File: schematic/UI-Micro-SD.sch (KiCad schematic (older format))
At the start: 30 parts, among them IC1 TCA9534PWR, J1 47309-3351, J2 Conn_02x04_Odd_Even, J3 Conn_02x05_Odd_Even, J4 Conn_02x03_Odd_Even, J5 Conn_02x08_Odd_Even, J6 Conn_01x08, J7 Conn_02x08_Odd_Even, J8 Solder-Jumper-3-3-3-Open, Q1 BSS138, U1 SFV14R-2STE1HLF, U2 DizzyBITLogo, U3 DizzyBIT-Layout

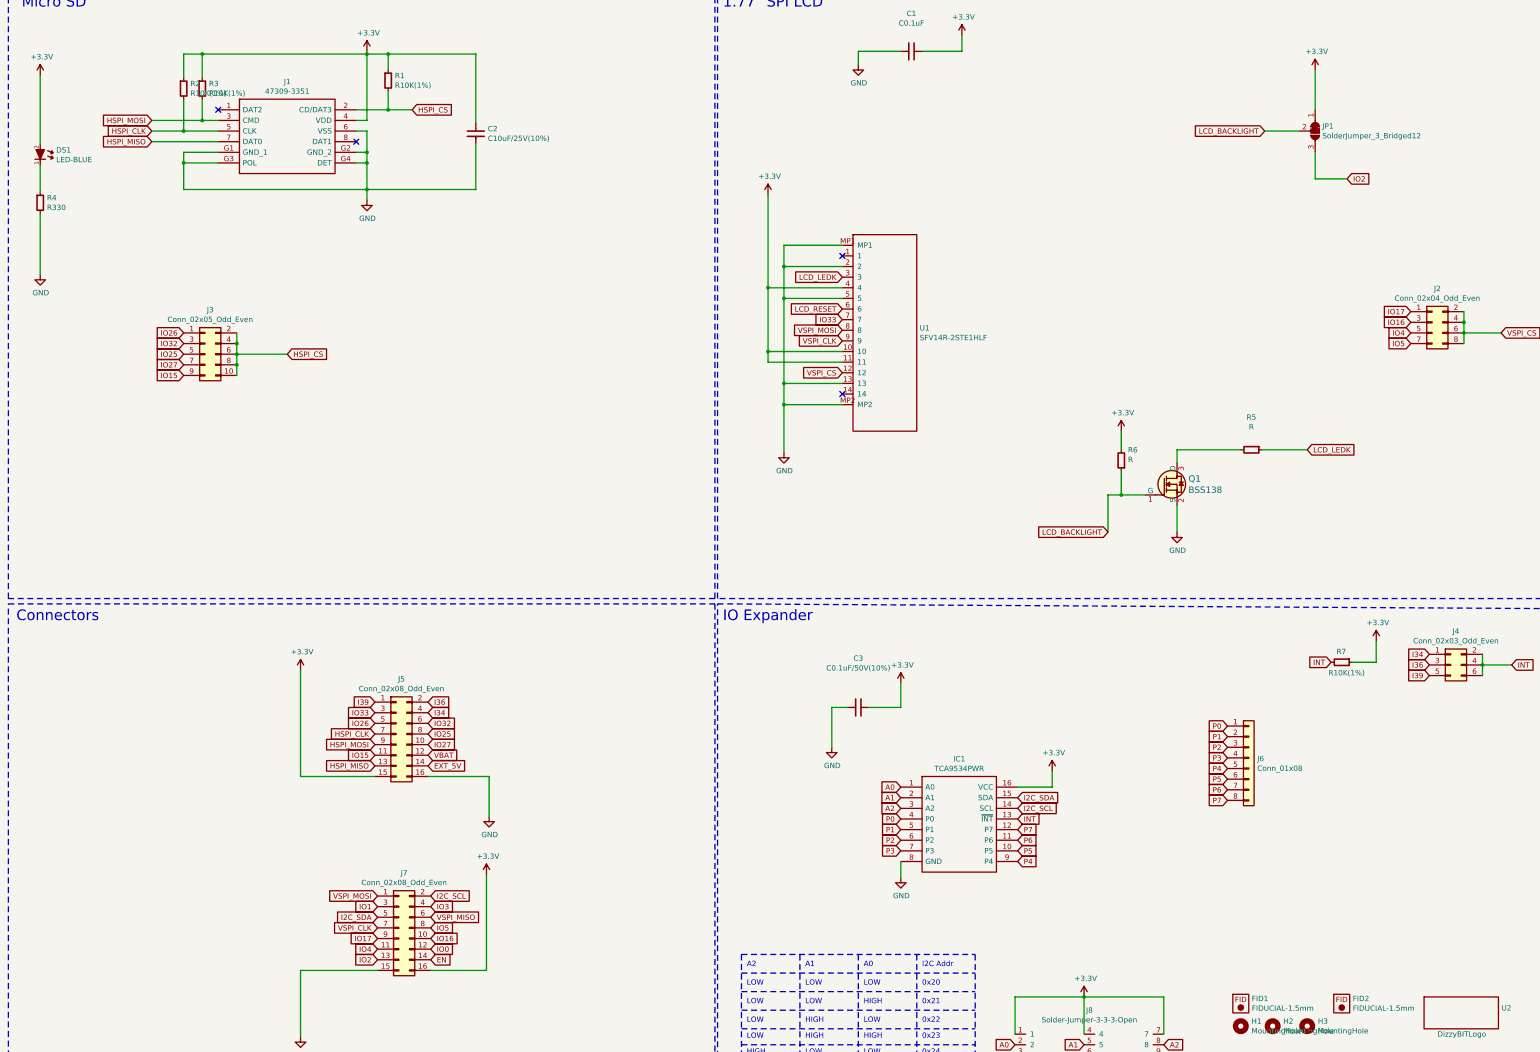
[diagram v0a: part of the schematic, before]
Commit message: Changed Connector designators
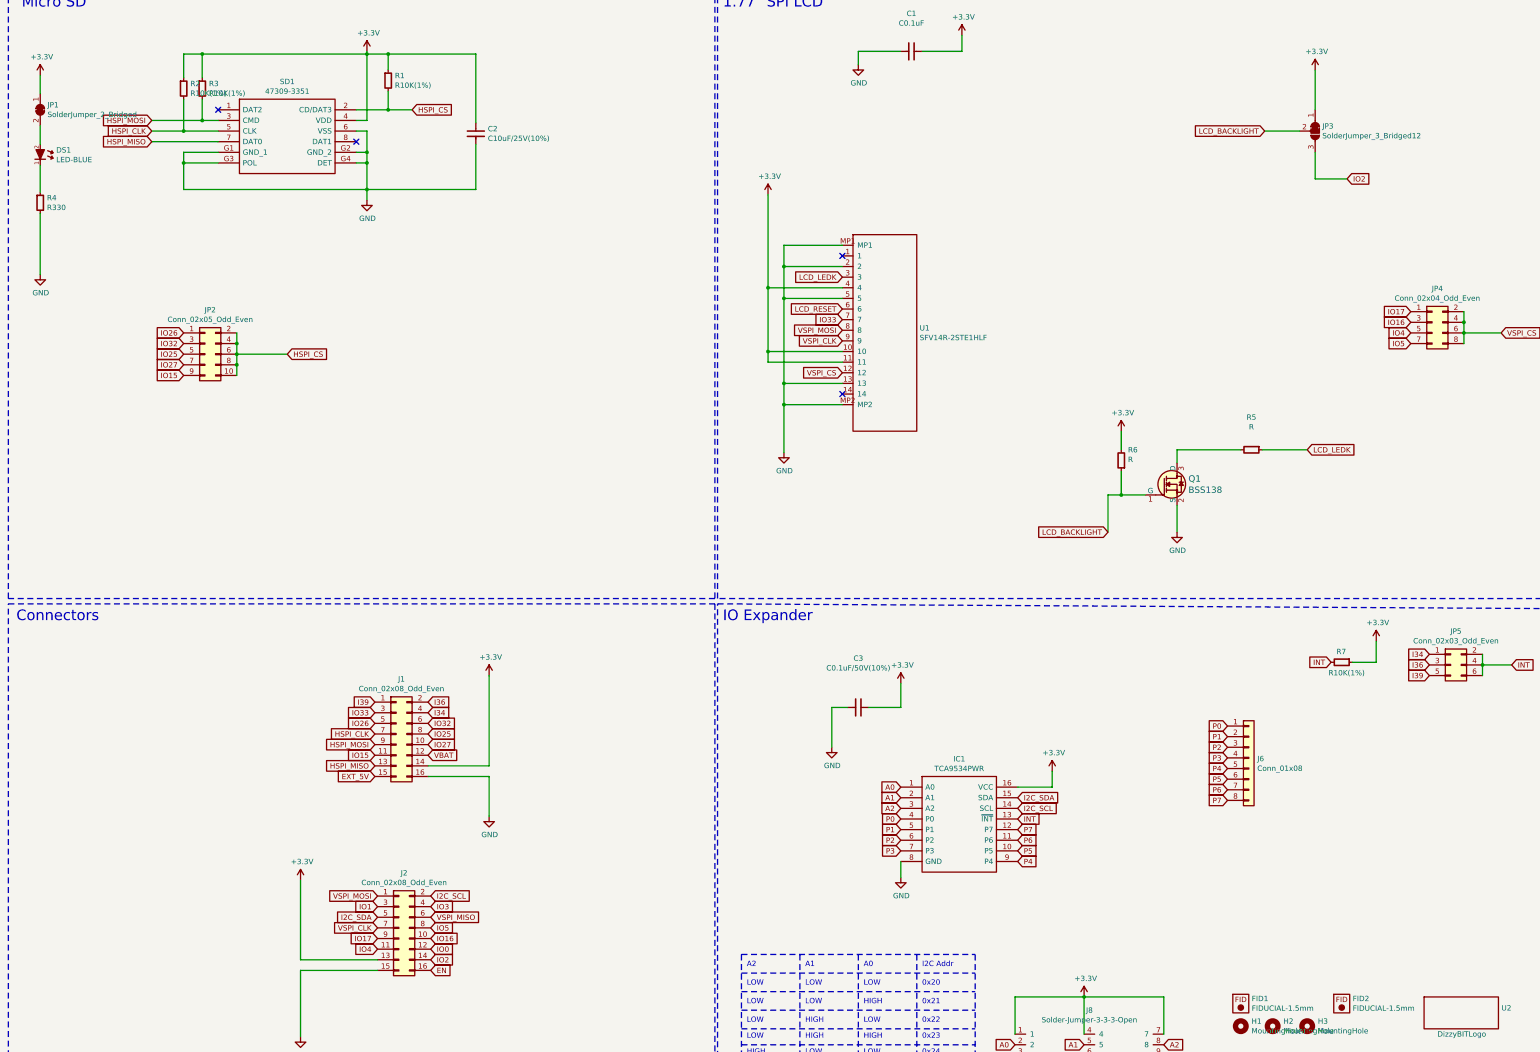
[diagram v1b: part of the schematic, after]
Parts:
- added JP1: SolderJumper_2_Bridged, symbol Jumper:SolderJumper_2_Bridged
- renumbered J5 to J1, J7 to J2, J3 to JP2, JP1 to JP3, J2 to JP4, J4 to JP5, J1 to SD1
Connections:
- net +3V3: now also J1.14 (Pin_14), J2.13 (Pin_13), JP1.1 (A); no longer DS1.2 (A), J1.15 (Pin_15), J2.16 (Pin_16)
- net EN: now also J2.16 (Pin_16); no longer J2.14 (Pin_14)
- net EXT_5V: now also J1.15 (Pin_15); no longer J1.14 (Pin_14)
- net IO2: now also J2.14 (Pin_14); no longer J2.13 (Pin_13)
- new net: DS1.2 (A), JP1.2 (B)
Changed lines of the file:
@@
 EESchema Schematic File Version 4
-LIBS:DizzyBit-MicroSD-cache
-LIBS:2-relay-over-io-cache
-LIBS:_DizzyBit-1.77LCD-cache
-LIBS:StandOut-2.0LCD-Keypad-cache
+LIBS:UI-Micro-SD-cache
 EELAYER 26 0
 EELAYER END
@@
 $EndComp
 Wire Wire Line
-	875  2050 875  1400
+	875  2050 875  1875
 $Comp
 L power:GND #PWR0102
@@
 	875  2250 875  2500
 $Comp
-L SamacSys_Parts:47309-3351 J1
+L SamacSys_Parts:47309-3351 SD1
 U 1 1 5C618E16
 P 2550 1725
-F 0 "J1" H 3200 1990 50  0000 C CNN
+F 0 "SD1" H 3200 1990 50  0000 C CNN
 F 1 "47309-3351" H 3200 1899 50  0000 C CNN
 F 2 "undo:Molex-MicroSD-473093351" H 3700 1825 50  0001 L CNN
@@
 VSPI_MOSI
 $Comp
-L Connector_Generic:Conn_02x08_Odd_Even J5
+L Connector_Generic:Conn_02x08_Odd_Even J1
 U 1 1 5D8B59AB
 P 4225 7600
-F 0 "J5" H 4275 8117 50  0000 C CNN
+F 0 "J1" H 4275 8117 50  0000 C CNN
 F 1 "Conn_02x08_Odd_Even" H 4275 8026 50  0000 C CNN
 F 2 "Connector_PinHeader_2.54mm:PinHeader_2x08_P2.54mm_Vertical" H 4225 7600 50  0001 C CNN
@@
 L power:+3.3V #PWR0105
 U 1 1 5D8B5B52
-P 3325 7000
-F 0 "#PWR0105" H 3325 6850 50  0001 C CNN
-F 1 "+3.3V" H 3340 7173 50  0000 C CNN
-F 2 "" H 3325 7000 50  0001 C CNN
-F 3 "" H 3325 7000 50  0001 C CNN
-	1    3325 7000
-	1    0    0    -1
-$EndComp
-Wire Wire Line
-	3325 8000 4025 8000
+P 5100 7050
+F 0 "#PWR0105" H 5100 6900 50  0001 C CNN
+F 1 "+3.3V" H 5115 7223 50  0000 C CNN
+F 2 "" H 5100 7050 50  0001 C CNN
+F 3 "" H 5100 7050 50  0001 C CNN
+	1    5100 7050
+	1    0    0    -1
+$EndComp
 $Comp
 L power:GND #PWR0106
@@
 L power:+3.3V #PWR0107
 U 1 1 5D8B5BF6
-P 5075 8925
-F 0 "#PWR0107" H 5075 8775 50  0001 C CNN
-F 1 "+3.3V" H 5090 9098 50  0000 C CNN
-F 2 "" H 5075 8925 50  0001 C CNN
-F 3 "" H 5075 8925 50  0001 C CNN
-	1    5075 8925
+P 3325 8975
+F 0 "#PWR0107" H 3325 8825 50  0001 C CNN
+F 1 "+3.3V" H 3340 9148 50  0000 C CNN
+F 2 "" H 3325 8975 50  0001 C CNN
+F 3 "" H 3325 8975 50  0001 C CNN
+	1    3325 8975
 	1    0    0    -1
 $EndComp
@@
 $EndComp
 Wire Wire Line
-	4550 9825 5075 9825
-Wire Wire Line
-	5075 9825 5075 8925
-Wire Wire Line
 	5100 8375 5100 8000
-Wire Wire Line
-	3325 8000 3325 7000
 Text GLabel 4050 9325 0    50   Input ~ 0
 I2C_SDA
@@
 Text GLabel 4050 9225 0    50   Input ~ 0
 IO1
-Text GLabel 4050 9725 0    50   Input ~ 0
+Text GLabel 4550 9725 2    50   Input ~ 0
 IO2
 Text GLabel 4550 9225 2    50   Input ~ 0
@@
 Text GLabel 4025 7300 0    50   Input ~ 0
 I39
-Text GLabel 4525 7900 2    50   Input ~ 0
+Text GLabel 4025 8000 0    50   Input ~ 0
 EXT_5V
 Wire Notes Line
@@
 Text GLabel 4525 7800 2    50   Input ~ 0
 VBAT
-Text GLabel 4550 9725 2    50   Input ~ 0
+Text GLabel 4550 9825 2    50   Input ~ 0
 EN
 $Comp
@@
 $EndComp
 $Comp
-L Connector_Generic:Conn_02x08_Odd_Even J7
+L Connector_Generic:Conn_02x08_Odd_Even J2
 U 1 1 5D8FF691
 P 4250 9425
-F 0 "J7" H 4300 9942 50  0000 C CNN
+F 0 "J2" H 4300 9942 50  0000 C CNN
 F 1 "Conn_02x08_Odd_Even" H 4300 9851 50  0000 C CNN
 F 2 "Connector_PinHeader_2.54mm:PinHeader_2x08_P2.54mm_Vertical" H 4250 9425 50  0001 C CNN
@@
 $EndComp
 $Comp
-L Connector_Generic:Conn_02x05_Odd_Even J3
+L Connector_Generic:Conn_02x05_Odd_Even JP2
 U 1 1 5D99A860
 P 2425 4025
-F 0 "J3" H 2475 4442 50  0000 C CNN
+F 0 "JP2" H 2475 4442 50  0000 C CNN
 F 1 "Conn_02x05_Odd_Even" H 2475 4351 50  0000 C CNN
 F 2 "DizzyBit:DizzyBit-SolderJumper-5-5-Open" H 2425 4025 50  0001 C CNN
@@
 	9550 1175 9550 1025
 $Comp
-L Jumper:SolderJumper_3_Bridged12 JP1
+L Jumper:SolderJumper_3_Bridged12 JP3
 U 1 1 5D7A4BED
 P 12875 1925
-F 0 "JP1" V 12829 1992 50  0000 L CNN
+F 0 "JP3" V 12829 1992 50  0000 L CNN
 F 1 "SolderJumper_3_Bridged12" V 12920 1992 50  0000 L CNN
 F 2 "DizzyBit:DizzyBit-SolderJumper-3-Open" H 12875 1925 50  0001 C CNN
@@
 	11450 10850 10700 10850
 $Comp
-L Connector_Generic:Conn_02x03_Odd_Even J4
+L Connector_Generic:Conn_02x03_Odd_Even JP5
 U 1 1 5DA1D4B1
 P 14150 6950
-F 0 "J4" H 14200 7267 50  0000 C CNN
+F 0 "JP5" H 14200 7267 50  0000 C CNN
 F 1 "Conn_02x03_Odd_Even" H 14200 7176 50  0000 C CNN
 F 2 "DizzyBit:DizzyBit-SolderJumper-3-3-Open" H 14150 6950 50  0001 C CNN
@@
 IO5
 $Comp
-L Connector_Generic:Conn_02x04_Odd_Even J2
+L Connector_Generic:Conn_02x04_Odd_Even JP4
 U 1 1 5DA528D6
 P 13975 3725
-F 0 "J2" H 14025 4042 50  0000 C CNN
+F 0 "JP4" H 14025 4042 50  0000 C CNN
 F 1 "Conn_02x04_Odd_Even" H 14025 3951 50  0000 C CNN
 F 2 "DizzyBit:DizzyBit-SolderJumper-4-4-Open" H 13975 3725 50  0001 C CNN
@@
 $EndComp
 $Comp
-L power:+3.3V #PWR?
+L power:+3.3V #PWR0122
 U 1 1 5DA6192C
 P 13450 6725
-F 0 "#PWR?" H 13450 6575 50  0001 C CNN
+F 0 "#PWR0122" H 13450 6575 50  0001 C CNN
 F 1 "+3.3V" H 13465 6898 50  0000 C CNN
 F 2 "" H 13450 6725 50  0001 C CNN
@@
 Wire Wire Line
 	13450 6925 13225 6925
+Wire Wire Line
+	5100 7050 5100 7900
+Wire Wire Line
+	5100 7900 4525 7900
+Wire Wire Line
+	3325 8975 3325 9725
+Wire Wire Line
+	3325 9725 4050 9725
+$Comp
+L Jumper:SolderJumper_2_Bridged JP1
+U 1 1 5D97861B
+P 875 1725
+F 0 "JP1" V 829 1793 50  0000 L CNN
+F 1 "SolderJumper_2_Bridged" V 920 1793 50  0000 L CNN
+F 2 "" H 875 1725 50  0001 C CNN
+F 3 "~" H 875 1725 50  0001 C CNN
+	1    875  1725
+	0    1    1    0
+$EndComp
+Wire Wire Line
+	875  1400 875  1575
 $EndSCHEMATC

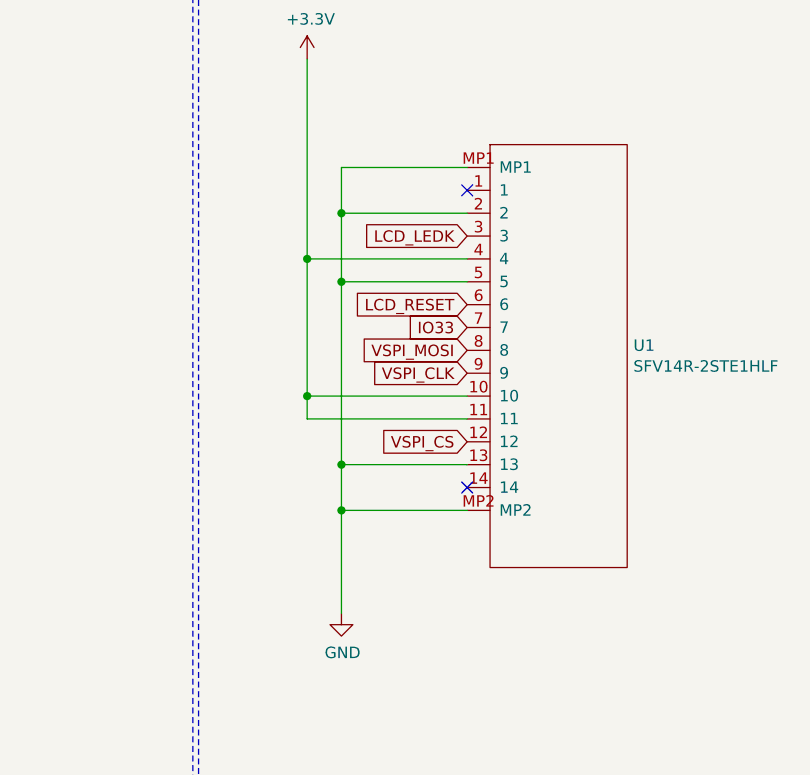
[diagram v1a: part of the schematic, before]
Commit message: Working on positioning the components
Changed the MicroSD footprint to match the connfly socket
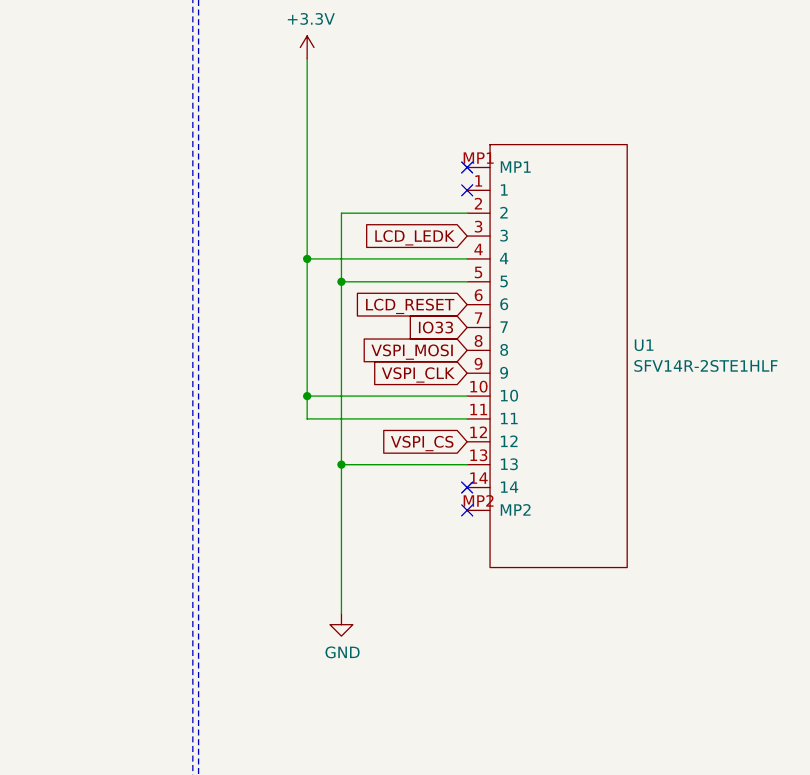
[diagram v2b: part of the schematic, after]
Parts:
- JP1: footprint (none) -> DizzyBit:DizzyBit-SolderJumper-2-Open
- SD1: footprint undo:Molex-MicroSD-473093351 -> Connfly:DS-1139-04
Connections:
- net GND: no longer U1.MP1, U1.MP2
- no-connect marks 4 -> 6
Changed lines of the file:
@@
 F 0 "SD1" H 3200 1990 50  0000 C CNN
 F 1 "47309-3351" H 3200 1899 50  0000 C CNN
-F 2 "undo:Molex-MicroSD-473093351" H 3700 1825 50  0001 L CNN
+F 2 "Connfly:DS-1139-04" H 3700 1825 50  0001 L CNN
 F 3 "https://componentsearchengine.com/Datasheets/1/47309-3351.pdf" H 3700 1725 50  0001 L CNN
 F 4 "WM10795DKR-ND" H 2550 1725 50  0001 C CNN "dk_pn"
@@
 	8425 4300 7875 4300
 Connection ~ 7875 4300
-Wire Wire Line
-	7875 4300 7875 4500
 $Comp
 L undo:SFV14R-2STE1HLF U1
@@
 	1    0    0    -1
 $EndComp
-Wire Wire Line
-	8425 3000 7875 3000
-Wire Wire Line
-	7875 3000 7875 3200
-Connection ~ 7875 3200
-Wire Wire Line
-	8425 4500 7875 4500
-Connection ~ 7875 4500
-Wire Wire Line
-	7875 4500 7875 4950
 Text GLabel 8425 3300 0    50   Input ~ 0
 LCD_LEDK
@@
 F 0 "JP1" V 829 1793 50  0000 L CNN
 F 1 "SolderJumper_2_Bridged" V 920 1793 50  0000 L CNN
-F 2 "" H 875 1725 50  0001 C CNN
+F 2 "DizzyBit:DizzyBit-SolderJumper-2-Open" H 875 1725 50  0001 C CNN
 F 3 "~" H 875 1725 50  0001 C CNN
 	1    875  1725
@@
 Wire Wire Line
 	875  1400 875  1575
+NoConn ~ 8425 3000
+Wire Wire Line
+	7875 4300 7875 4950
+NoConn ~ 8425 4500
 $EndSCHEMATC
